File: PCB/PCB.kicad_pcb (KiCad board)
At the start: 4 copper layers, 54 x 29 mm, 92 parts, among them J1 USB_B_Micro, Q1 PJA3428, Q2 PJA3428, Q3 AO3401A, SW1 SW_Push, SW2 SW_Push, SW3 SW_Push, SW4 ON/OFF, U1 ESP32-PICO-MINI-02, U2 CP2102N-Axx-xQFN24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

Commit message: update
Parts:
- moved D5 0.52 mm to (224.8, 92.9)
- moved R19 0.52 mm to (225.2, 94.8)
- moved TP3 0.22 mm to (222.6, 95.0)
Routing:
- net Vin: track 9.02 -> 6.09 mm
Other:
- board text added: "Power"
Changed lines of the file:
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@@
     (property "Sheetname" "")
     (attr smd)
-    (fp_text reference "C7" (at 0 -1.5) (layer "F.SilkS")
+    (fp_text reference "C7" (at -0.45 1.7) (layer "F.SilkS")
       (effects (font (size 0.5 0.5) (thickness 0.1)))
     )
@@
   )
   (footprint "LED_SMD:LED_0805_2012Metric_Pad1.15x1.40mm_HandSolder" (layer "F.Cu")
-    (at 224.9 92.4 180)
+    (at 224.75 92.9 180)
     (descr "LED SMD 0805 (2012 Metric), square (rectangular) end terminal, IPC_7351 nominal, (Body size source: https://docs.google.com/spreadsheets/d/1BsfQQcO9C6DZCsRaXUlFlo91Tg2WpOkGARC1WS5S8t0/edit?usp=sharing), generated with kicad-footprint-generator")
     (tags "LED handsolder")
@@
     (property "Sheetname" "")
     (attr smd)
-    (fp_text reference "D5" (at 2.4 0) (layer "F.SilkS")
+    (fp_text reference "D5" (at 0.45 2.65) (layer "F.SilkS")
       (effects (font (size 0.5 0.5) (thickness 0.1)))
     )
@@
   )
   (footprint "Resistor_SMD:R_0603_1608Metric" (layer "F.Cu")
-    (at 225.325 94.25 180)
+    (at 225.175 94.75 180)
     (descr "Resistor SMD 0603 (1608 Metric), square (rectangular) end terminal, IPC_7351 nominal, (Body size source: IPC-SM-782 page 72, https://www.pcb-3d.com/wordpress/wp-content/uploads/ipc-sm-782a_amendment_1_and_2.pdf), generated with kicad-footprint-generator")
     (tags "resistor")
@@
     (property "Sheetname" "")
     (attr smd)
-    (fp_text reference "R19" (at -0.375 -1.15) (layer "F.SilkS")
+    (fp_text reference "R19" (at -0.125 5.4) (layer "F.SilkS")
       (effects (font (size 0.5 0.5) (thickness 0.1)))
     )
@@
   )
   (footprint "TestPoint:TestPoint_Pad_D1.0mm" (layer "F.Cu")
-    (at 222.725 94.775)
+    (at 222.6 94.95)
     (descr "SMD pad as test Point, diameter 1.0mm")
     (tags "test point SMD pad")
@@
   (gr_line (start 240.453993 110.15) (end 240.628993 110.35) (layer "F.SilkS") (width 0.15))
   (gr_line (start 238.903993 108.575) (end 238.953993 108.725) (layer "F.SilkS") (width 0.15))
+  (gr_circle (center 226.8 92.05) (end 226.85 92.05) (layer "F.SilkS") (width 0.15) (fill none))
   (gr_line (start 240.403993 110.35) (end 240.853993 110.35) (layer "F.SilkS") (width 0.15))
   (gr_line (start 240.403993 110.7) (end 240.403993 110.05) (layer "F.SilkS") (width 0.15))
@@
     (effects (font (size 0.7 0.7) (thickness 0.15)))
   )
-  (gr_text "VIN" (at 222.25 93.35) (layer "F.SilkS")
+  (gr_text "VIN" (at 221.4 96.15) (layer "F.SilkS")
     (effects (font (size 0.7 0.7) (thickness 0.15)))
   )
@@
     (effects (font (size 0.7 0.7) (thickness 0.15)))
   )
+  (gr_text "Power" (at 224.75 91.4) (layer "F.SilkS")
+    (effects (font (size 0.7 0.7) (thickness 0.15)))
+  )
   (gr_text "RTS\n" (at 229.7 112.55) (layer "F.SilkS")
     (effects (font (size 0.7 0.7) (thickness 0.15)))
@@
   (segment (start 233.752999 102.568853) (end 234.227125 103.042979) (width 0.25) (layer "B.Cu") (net 15))
   (segment (start 232.707275 102.568853) (end 233.752999 102.568853) (width 0.25) (layer "B.Cu") (net 15))
-  (segment (start 223.375 95.425) (end 222.725 94.775) (width 0.35) (layer "F.Cu") (net 26))
+  (segment (start 223.25 95.6) (end 222.6 94.95) (width 0.35) (layer "F.Cu") (net 26))
   (segment (start 227.795 97.2) (end 225.975 97.2) (width 0.35) (layer "F.Cu") (net 26))
-  (segment (start 224.975 95.425) (end 223.375 95.425) (width 0.35) (layer "F.Cu") (net 26))
-  (segment (start 226.15 94.25) (end 224.975 95.425) (width 0.35) (layer "F.Cu") (net 26))
-  (segment (start 226.15 94.25) (end 226.15 97.025) (width 0.35) (layer "F.Cu") (net 26))
+  (segment (start 225.7 94.75) (end 226 94.75) (width 0.25) (layer "F.Cu") (net 26))
+  (segment (start 224.85 95.6) (end 223.25 95.6) (width 0.35) (layer "F.Cu") (net 26))
   (segment (start 226.15 97.025) (end 225.975 97.2) (width 0.35) (layer "F.Cu") (net 26))
+  (segment (start 224.85 95.6) (end 225.7 94.75) (width 0.25) (layer "F.Cu") (net 26))
   (segment (start 195.01 108.97) (end 196.22 108.97) (width 0.25) (layer "F.Cu") (net 27))
   (segment (start 196.22 108.97) (end 196.675 109.425) (width 0.25) (layer "F.Cu") (net 27))
@@
   (segment (start 224.8 113.275) (end 224.8 113.025) (width 0.3) (layer "B.Cu") (net 30))
   (segment (start 244.31 110.48) (end 244.31 109.41) (width 0.25) (layer "B.Cu") (net 30))
-  (segment (start 223.875 93.625) (end 224.5 94.25) (width 0.25) (layer "F.Cu") (net 31))
-  (segment (start 223.875 92.4) (end 223.875 93.625) (width 0.25) (layer "F.Cu") (net 31))
+  (segment (start 223.725 94.125) (end 224.35 94.75) (width 0.25) (layer "F.Cu") (net 31))
+  (segment (start 223.725 92.9) (end 223.725 94.125) (width 0.25) (layer "F.Cu") (net 31))
   (segment (start 217.69813 109.576677) (end 217.224807 110.05) (width 0.25) (layer "F.Cu") (net 32))
   (segment (start 215.6 103.55) (end 215.6 104.924245) (width 0.25) (layer "F.Cu") (net 32))
@@
   (segment (start 230.649999 97.044999) (end 230.805 97.2) (width 0.35) (layer "F.Cu") (net 70))
   (segment (start 230.649999 94.748401) (end 230.649999 97.044999) (width 0.35) (layer "F.Cu") (net 70))
+  (segment (start 228.95 92.9) (end 229.25 92.6) (width 0.25) (layer "F.Cu") (net 74))
   (segment (start 216.4 113.8) (end 215.6 113.8) (width 0.25) (layer "F.Cu") (net 74))
   (segment (start 192.52 111.81) (end 192.52 113.375) (width 0.25) (layer "F.Cu") (net 74))
@@
   (segment (start 235.225 98.875) (end 236.325 99.975) (width 0.35) (layer "F.Cu") (net 74))
   (segment (start 196.0575 113.1825) (end 195.35 112.475) (width 0.25) (layer "F.Cu") (net 74))
-  (segment (start 229.120199 92.729801) (end 226.254801 92.729801) (width 0.35) (layer "F.Cu") (net 74))
   (segment (start 200.374046 114.1825) (end 199.4929 113.301354) (width 0.25) (layer "F.Cu") (net 74))
   (segment (start 219.45 112.1) (end 219.45 112.9) (width 0.25) (layer "F.Cu") (net 74))
   (segment (start 219.1 104) (end 219.15 103.95) (width 0.25) (layer "F.Cu") (net 74))
-  (segment (start 226.254801 92.729801) (end 225.925 92.4) (width 0.35) (layer "F.Cu") (net 74))
   (segment (start 222.65 107.775) (end 225.304316 107.775) (width 0.25) (layer "F.Cu") (net 74))
   (segment (start 239.4 95.39) (end 238.2975 95.39) (width 0.35) (layer "F.Cu") (net 74))
   (segment (start 210 113.8) (end 210.8 113.8) (width 0.25) (layer "F.Cu") (net 74))
   (segment (start 196.3375 114.6825) (end 196.3375 115.4325) (width 0.25) (layer "F.Cu") (net 74))
+  (segment (start 225.775 92.9) (end 228.95 92.9) (width 0.25) (layer "F.Cu") (net 74))
   (segment (start 201.5625 114.1825) (end 200.374046 114.1825) (width 0.25) (layer "F.Cu") (net 74))
   (segment (start 214.8 111.2) (end 215.15 110.85) (width 0.25) (layer "F.Cu") (net 74))

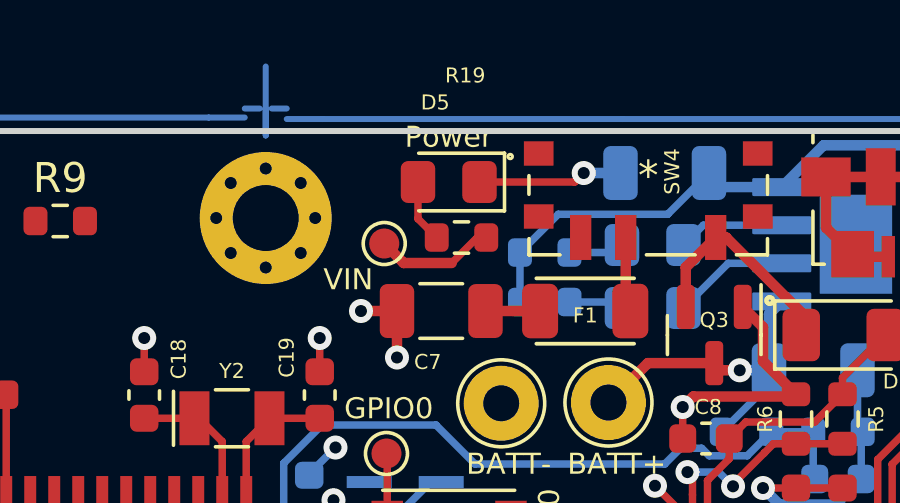
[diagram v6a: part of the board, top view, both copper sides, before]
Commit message: update the very silky screen
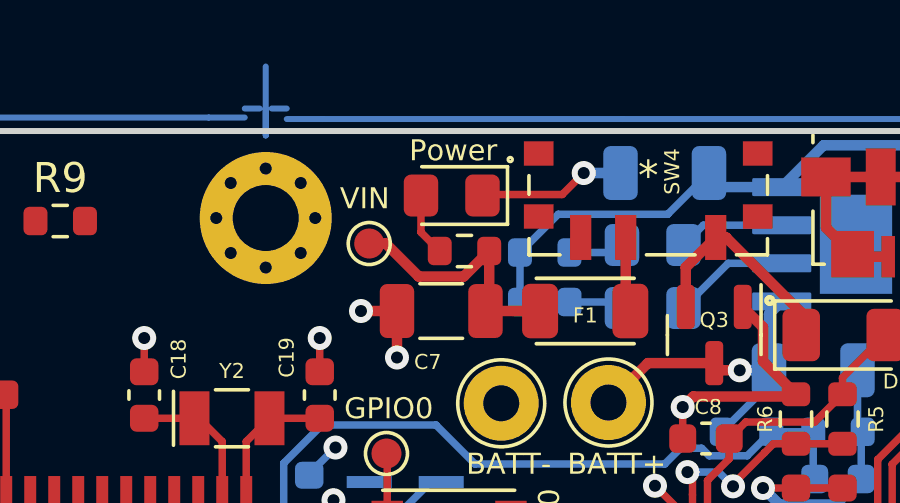
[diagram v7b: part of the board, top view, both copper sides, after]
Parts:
- moved TP3 0.50 mm to (222.1, 95.0)
- moved R19 0.46 mm to (225.3, 95.2)
- moved D5 0.46 mm to (224.8, 93.3)
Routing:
- net Vin: track 6.09 -> 8.93 mm
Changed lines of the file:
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@@
   )
   (footprint "LED_SMD:LED_0805_2012Metric_Pad1.15x1.40mm_HandSolder" (layer "F.Cu")
-    (at 224.75 92.9 180)
+    (at 224.85 93.35 180)
     (descr "LED SMD 0805 (2012 Metric), square (rectangular) end terminal, IPC_7351 nominal, (Body size source: https://docs.google.com/spreadsheets/d/1BsfQQcO9C6DZCsRaXUlFlo91Tg2WpOkGARC1WS5S8t0/edit?usp=sharing), generated with kicad-footprint-generator")
     (tags "LED handsolder")
@@
     (property "Sheetname" "")
     (attr smd)
-    (fp_text reference "D5" (at 0.45 2.65) (layer "F.SilkS")
+    (fp_text reference "D5" (at 0.45 2.65) (layer "F.Fab")
       (effects (font (size 0.5 0.5) (thickness 0.1)))
     )
@@
   )
   (footprint "Resistor_SMD:R_0603_1608Metric" (layer "F.Cu")
-    (at 225.175 94.75 180)
+    (at 225.275 95.2 180)
     (descr "Resistor SMD 0603 (1608 Metric), square (rectangular) end terminal, IPC_7351 nominal, (Body size source: IPC-SM-782 page 72, https://www.pcb-3d.com/wordpress/wp-content/uploads/ipc-sm-782a_amendment_1_and_2.pdf), generated with kicad-footprint-generator")
     (tags "resistor")
@@
     (property "Sheetname" "")
     (attr smd)
-    (fp_text reference "R19" (at -0.125 5.4) (layer "F.SilkS")
+    (fp_text reference "R19" (at -0.125 5.4) (layer "F.Fab")
       (effects (font (size 0.5 0.5) (thickness 0.1)))
     )
@@
   )
   (footprint "TestPoint:TestPoint_Pad_D1.0mm" (layer "F.Cu")
-    (at 222.6 94.95)
+    (at 222.1 94.95)
     (descr "SMD pad as test Point, diameter 1.0mm")
     (tags "test point SMD pad")
@@
   (gr_line (start 240.453993 110.15) (end 240.628993 110.35) (layer "F.SilkS") (width 0.15))
   (gr_line (start 238.903993 108.575) (end 238.953993 108.725) (layer "F.SilkS") (width 0.15))
-  (gr_circle (center 226.8 92.05) (end 226.85 92.05) (layer "F.SilkS") (width 0.15) (fill none))
+  (gr_circle (center 226.8 92.15) (end 226.85 92.15) (layer "F.SilkS") (width 0.15) (fill none))
   (gr_line (start 240.403993 110.35) (end 240.853993 110.35) (layer "F.SilkS") (width 0.15))
   (gr_line (start 240.403993 110.7) (end 240.403993 110.05) (layer "F.SilkS") (width 0.15))
@@
     (effects (font (size 0.7 0.7) (thickness 0.15)))
   )
-  (gr_text "VIN" (at 221.4 96.15) (layer "F.SilkS")
+  (gr_text "VIN" (at 221.95 93.45) (layer "F.SilkS")
     (effects (font (size 0.7 0.7) (thickness 0.15)))
   )
@@
     (effects (font (size 0.7 0.7) (thickness 0.15)))
   )
-  (gr_text "Power" (at 224.75 91.4) (layer "F.SilkS")
+  (gr_text "Power" (at 224.9 91.85) (layer "F.SilkS")
     (effects (font (size 0.7 0.7) (thickness 0.15)))
   )
@@
   (segment (start 233.752999 102.568853) (end 234.227125 103.042979) (width 0.25) (layer "B.Cu") (net 15))
   (segment (start 232.707275 102.568853) (end 233.752999 102.568853) (width 0.25) (layer "B.Cu") (net 15))
-  (segment (start 223.25 95.6) (end 222.6 94.95) (width 0.35) (layer "F.Cu") (net 26))
   (segment (start 227.795 97.2) (end 225.975 97.2) (width 0.35) (layer "F.Cu") (net 26))
-  (segment (start 225.7 94.75) (end 226 94.75) (width 0.25) (layer "F.Cu") (net 26))
-  (segment (start 224.85 95.6) (end 223.25 95.6) (width 0.35) (layer "F.Cu") (net 26))
+  (segment (start 226.1 97.075) (end 225.975 97.2) (width 0.35) (layer "F.Cu") (net 26))
+  (segment (start 223.75 96.05) (end 222.65 94.95) (width 0.35) (layer "F.Cu") (net 26))
+  (segment (start 226.1 95.2) (end 226.1 97.075) (width 0.35) (layer "F.Cu") (net 26))
+  (segment (start 222.65 94.95) (end 222.1 94.95) (width 0.35) (layer "F.Cu") (net 26))
+  (segment (start 226.1 95.2) (end 225.25 96.05) (width 0.35) (layer "F.Cu") (net 26))
+  (segment (start 225.25 96.05) (end 223.75 96.05) (width 0.35) (layer "F.Cu") (net 26))
   (segment (start 226.15 97.025) (end 225.975 97.2) (width 0.35) (layer "F.Cu") (net 26))
-  (segment (start 224.85 95.6) (end 225.7 94.75) (width 0.25) (layer "F.Cu") (net 26))
   (segment (start 195.01 108.97) (end 196.22 108.97) (width 0.25) (layer "F.Cu") (net 27))
   (segment (start 196.22 108.97) (end 196.675 109.425) (width 0.25) (layer "F.Cu") (net 27))
@@
   (segment (start 224.8 113.275) (end 224.8 113.025) (width 0.3) (layer "B.Cu") (net 30))
   (segment (start 244.31 110.48) (end 244.31 109.41) (width 0.25) (layer "B.Cu") (net 30))
-  (segment (start 223.725 94.125) (end 224.35 94.75) (width 0.25) (layer "F.Cu") (net 31))
-  (segment (start 223.725 92.9) (end 223.725 94.125) (width 0.25) (layer "F.Cu") (net 31))
+  (segment (start 223.825 94.575) (end 224.45 95.2) (width 0.25) (layer "F.Cu") (net 31))
+  (segment (start 223.825 93.35) (end 223.825 94.575) (width 0.25) (layer "F.Cu") (net 31))
   (segment (start 217.69813 109.576677) (end 217.224807 110.05) (width 0.25) (layer "F.Cu") (net 32))
   (segment (start 215.6 103.55) (end 215.6 104.924245) (width 0.25) (layer "F.Cu") (net 32))
@@
   (segment (start 230.649999 97.044999) (end 230.805 97.2) (width 0.35) (layer "F.Cu") (net 70))
   (segment (start 230.649999 94.748401) (end 230.649999 97.044999) (width 0.35) (layer "F.Cu") (net 70))
-  (segment (start 228.95 92.9) (end 229.25 92.6) (width 0.25) (layer "F.Cu") (net 74))
   (segment (start 216.4 113.8) (end 215.6 113.8) (width 0.25) (layer "F.Cu") (net 74))
   (segment (start 192.52 111.81) (end 192.52 113.375) (width 0.25) (layer "F.Cu") (net 74))
@@
   (segment (start 210 113.8) (end 210.8 113.8) (width 0.25) (layer "F.Cu") (net 74))
   (segment (start 196.3375 114.6825) (end 196.3375 115.4325) (width 0.25) (layer "F.Cu") (net 74))
-  (segment (start 225.775 92.9) (end 228.95 92.9) (width 0.25) (layer "F.Cu") (net 74))
   (segment (start 201.5625 114.1825) (end 200.374046 114.1825) (width 0.25) (layer "F.Cu") (net 74))
   (segment (start 214.8 111.2) (end 215.15 110.85) (width 0.25) (layer "F.Cu") (net 74))
@@
   (segment (start 244.4 97.225) (end 244.4 97.65) (width 0.25) (layer "F.Cu") (net 74))
   (segment (start 198.111754 114.6825) (end 196.3375 114.6825) (width 0.25) (layer "F.Cu") (net 74))
+  (segment (start 225.908 93.317) (end 228.533 93.317) (width 0.25) (layer "F.Cu") (net 74))
   (segment (start 222.675 106) (end 222.675 105.775) (width 0.25) (layer "F.Cu") (net 74))
   (segment (start 220.45 99.225) (end 220.45 98.1) (width 0.25) (layer "F.Cu") (net 74))
@@
   (segment (start 211.6 111.2) (end 211.25 110.85) (width 0.25) (layer "F.Cu") (net 74))
   (segment (start 232.55 101.45) (end 232.55 100.4) (width 0.25) (layer "F.Cu") (net 74))
+  (segment (start 225.875 93.35) (end 225.908 93.317) (width 0.25) (layer "F.Cu") (net 74))
   (segment (start 221.625 113.525) (end 223.2 113.525) (width 0.3) (layer "F.Cu") (net 74))
   (segment (start 237.875 103.1) (end 236.325 103.1) (width 0.25) (layer "F.Cu") (net 74))
@@
   (segment (start 202.385 108.945) (end 202.385 109.77) (width 0.25) (layer "F.Cu") (net 74))
   (segment (start 243.1875 95.305) (end 243.1875 95.063) (width 0.35) (layer "F.Cu") (net 74))
+  (segment (start 228.533 93.317) (end 229.25 92.6) (width 0.25) (layer "F.Cu") (net 74))
   (segment (start 237.325 92.73) (end 237.325 94.4175) (width 0.35) (layer "F.Cu") (net 74))
   (segment (start 211.6 113.8) (end 212.4 113.8) (width 0.25) (layer "F.Cu") (net 74))

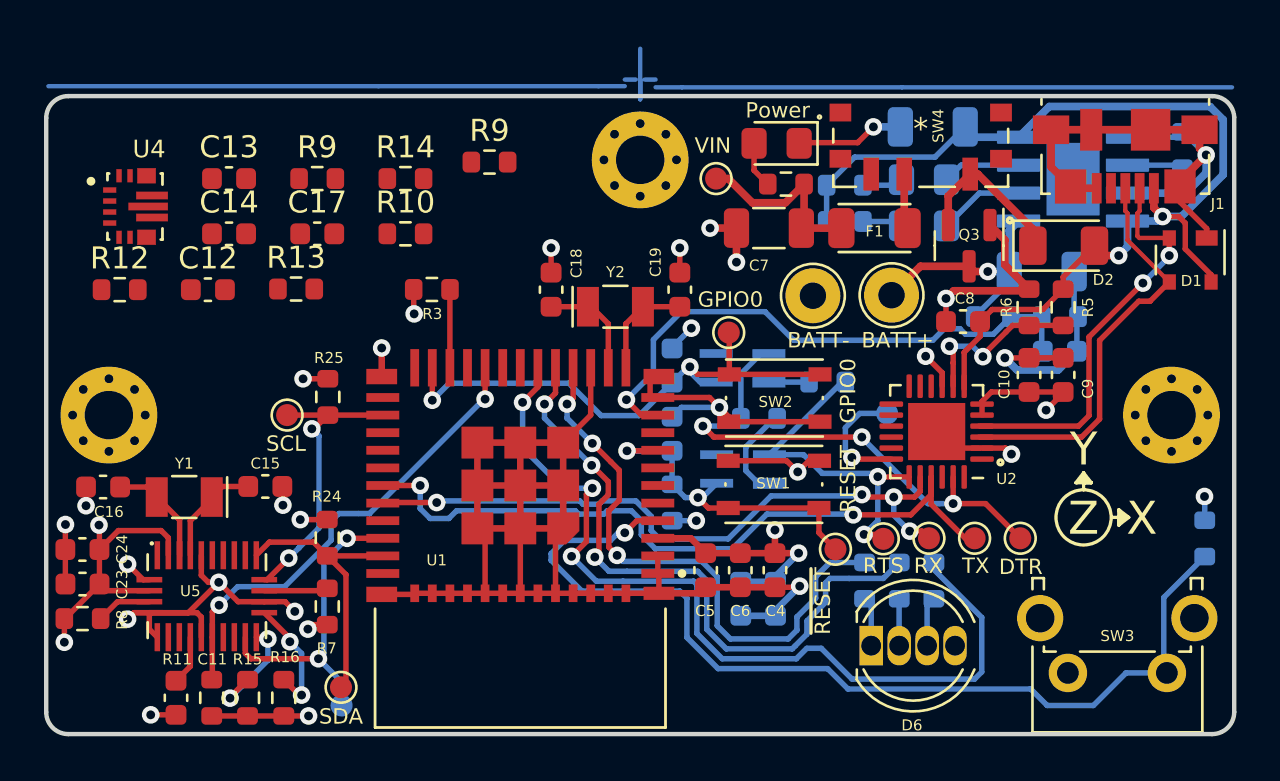
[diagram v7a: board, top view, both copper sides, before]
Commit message: update power connector and silkscreen
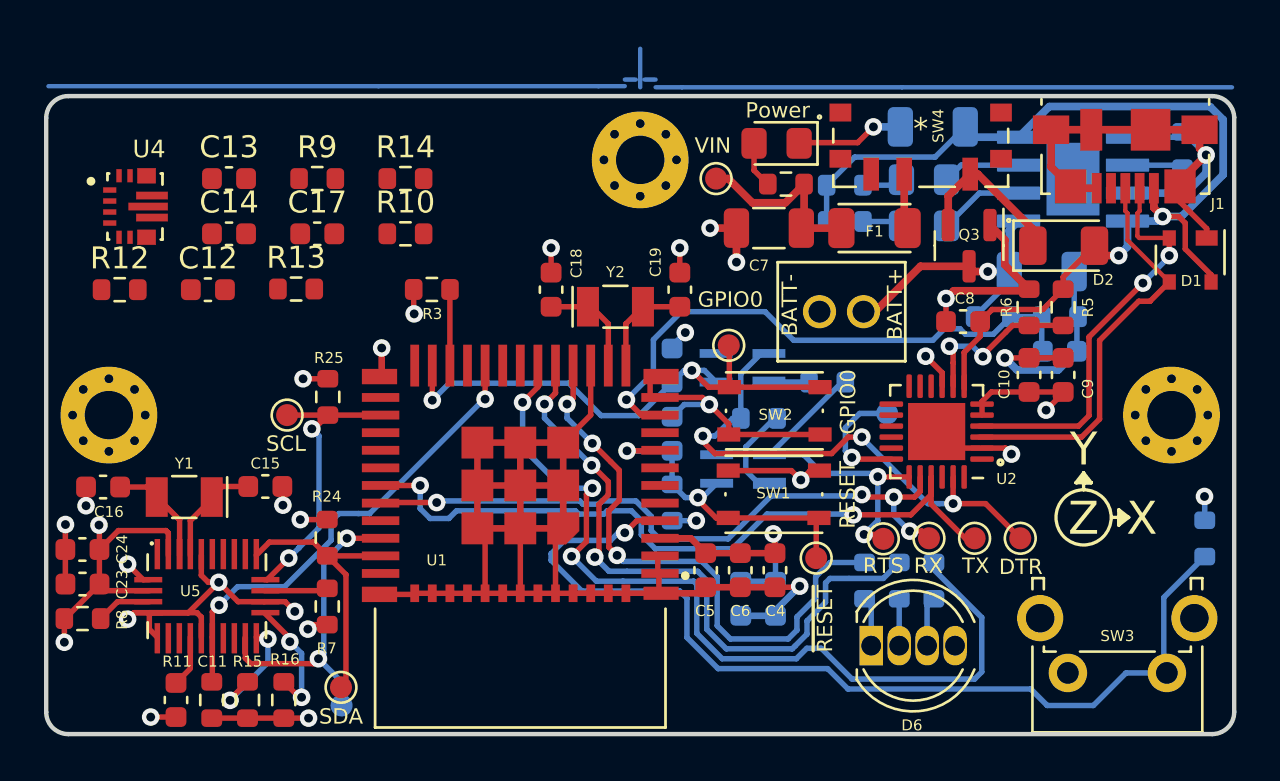
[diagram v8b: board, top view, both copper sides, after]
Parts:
- removed the R9 at (211.8, 94.2)
- removed TP10: BatteryPlusPad, TestPoint:TestPoint_THTPad_D2.5mm_Drill1.2mm
- removed TP9: BatteryMinusPad, TestPoint:TestPoint_THTPad_D2.5mm_Drill1.2mm
- added J2: Conn_01x02, PHR-2:JST_PHR-2, F.Cu at (227.8, 101.0)
- moved TP11 0.96 mm to (226.7, 112.2)
- moved SW2 0.58 mm to (224.8, 105.5)
- moved TP12 0.58 mm to (222.7, 102.5)
- moved SW1 0.45 mm to (224.7, 109.3)
- moved C11 0.10 mm to (197.6, 118.7)
- moved R11 0.10 mm to (199.2, 118.7)
- moved R15 0.10 mm to (200.8, 118.7)
- moved R16 0.10 mm to (202.4, 118.7)
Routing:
- net +BATT: track 11.2 -> 12.8 mm
- net BNO_INTERRUPT: track 14.4 -> 15.4 mm
- net GND: track 161.3 -> 160.3 mm
- net PROG_DTR: track 23.3 -> 24.1 mm
- net +3.3V: track 41.4 -> 40.8 mm, vias 12 -> 11
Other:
- board text added: "Charge"
- board text added: "Full"
